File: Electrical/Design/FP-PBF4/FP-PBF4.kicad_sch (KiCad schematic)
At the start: 21 parts

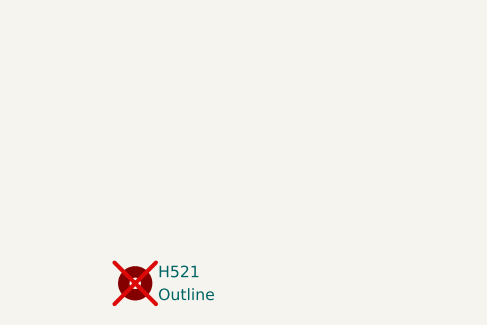
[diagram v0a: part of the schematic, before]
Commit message: SUKU frontpanel hatch pattern updated, outline updated, silk screen updated
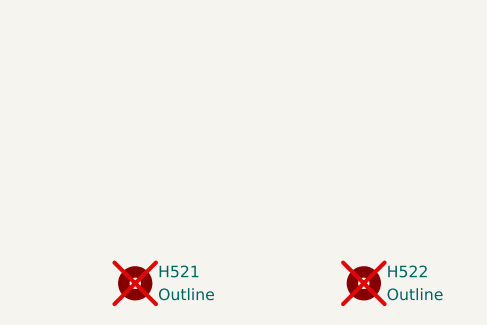
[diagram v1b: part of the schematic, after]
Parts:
- added H522: Outline, suku_basics:OSHWA, symbol Mechanical:MountingHole
- H521: footprint suku_basics:FP_OUTLINE -> suku_basics:FP_OUTLINE_2
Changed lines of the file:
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@@
+	(symbol
+		(lib_id "Mechanical:MountingHole")
+		(at 177.8 203.2 0)
+		(unit 1)
+		(exclude_from_sim yes)
+		(in_bom no)
+		(on_board yes)
+		(dnp yes)
+		(fields_autoplaced yes)
+		(property "Reference" "H522"
+			(at 180.34 201.9299 0)
+			(effects
+				(font
+					(size 1.27 1.27)
+				)
+				(justify left)
+			)
+		)
+		(property "Value" "Outline"
+			(at 180.34 204.4699 0)
+			(effects
+				(font
+					(size 1.27 1.27)
+				)
+				(justify left)
+			)
+		)
+		(property "Footprint" "suku_basics:OSHWA"
+			(at 177.8 203.2 0)
+			(effects
+				(font
+					(size 1.27 1.27)
+				)
+				(hide yes)
+			)
+		)
+		(property "Datasheet" "~"
+			(at 177.8 203.2 0)
+			(effects
+				(font
+					(size 1.27 1.27)
+				)
+				(hide yes)
+			)
+		)
+		(property "Description" "Mounting Hole without connection"
+			(at 177.8 203.2 0)
+			(effects
+				(font
+					(size 1.27 1.27)
+				)
+				(hide yes)
+			)
+		)
+		(instances
+			(project "FP-PBF4"
+				(path "/e5217a0c-7f55-4c30-adda-7f8d95709d1b"
+					(reference "H522")
+					(unit 1)
+				)
+			)
+		)
+	)
 	(symbol
 		(lib_id "Mechanical:MountingHole")
@@
 			)
 		)
-		(property "Footprint" "suku_basics:FP_OUTLINE"
+		(property "Footprint" "suku_basics:FP_OUTLINE_2"
 			(at 152.4 203.2 0)
 			(effects

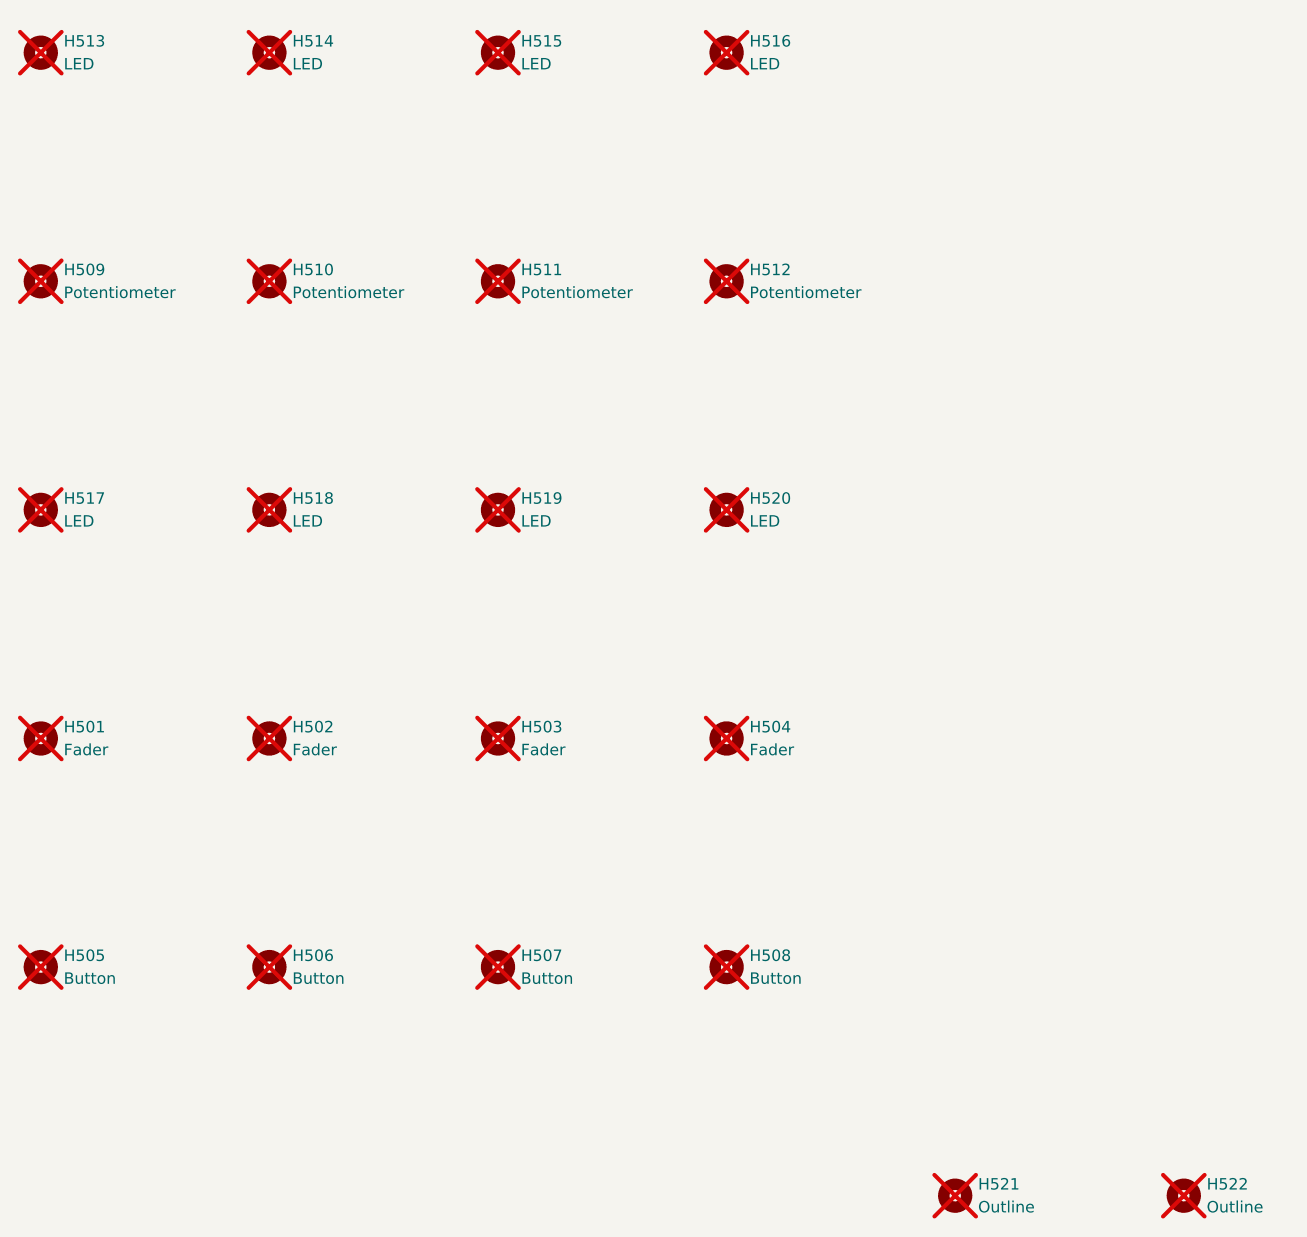
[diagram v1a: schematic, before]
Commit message: SUKU PBF4 frontpanel updated to use plated lightpipe
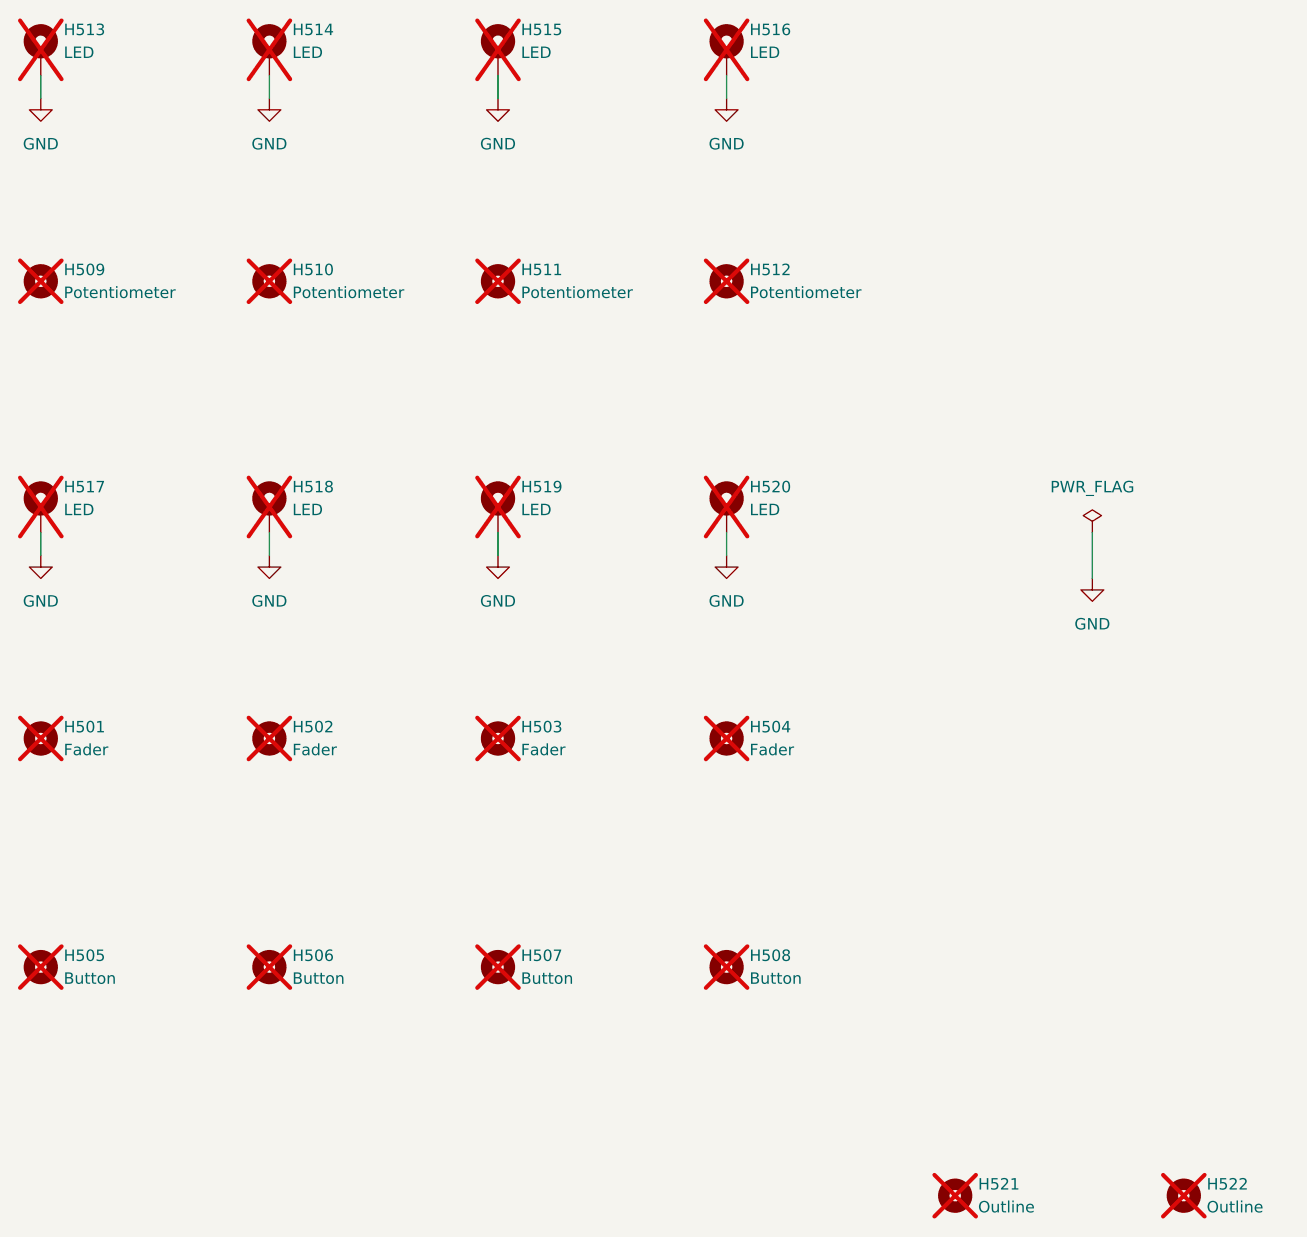
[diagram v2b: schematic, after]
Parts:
- H513, H514, H515, H516, H517, H518, H519, H520: footprint suku_basics:FP_LED -> suku_basics:FP_LED_TIGHT; symbol Mechanical:MountingHole -> Mechanical:MountingHole_Pad
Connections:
- new net GND: H513.1, H514.1, H515.1, H516.1, H517.1, H518.1, H519.1, H520.1
